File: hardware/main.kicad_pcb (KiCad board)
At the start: 4 copper layers, 57 x 93 mm, 398 parts, among them J1 DS1128-09-S8B8X, J2 DS1128-09-S8B8X, J3 DS1128-09-S8B8X, J4 98424-G52-04ALF, J5 Bus_PCI_Express_Mini, J6 IDC-08M, J7 IDC-08M, J8 USB_C_Receptacle, J9 TYPE-C-31-M-12, Q1 SSM6J501NU, Q2 SSM6J501NU, Q3 FDV301N, Q4 BC817, SW1 TS-1187A-B-A-B, SW2 TS-1187A-B-A-B, SW3 TS-1187A-B-A-B, SW4 TS-1187A-B-A-B, U1 SN74LVC1G175, U10 W25Q256FVEIG, U12 TPD2EUSB30, U13 TPD2EUSB30, U14 TPD2EUSB30, U15 IP5328P, U16 N096-2864KSWEG01-H30, U2 MT7621A, U3 TPS63020, U4 TPS63020, U5 MT3420B, U6 MT3420B, U7 MT3420B, U8 MT3420B, U9 NT5CB64M16FP-DH (!), Y1 X322540MPB4SI

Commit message: add mPCI-e and m2 conn
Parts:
- added J10: AS0BC21-S30BM-7H, MAS_Package_std:Bus_M.2_Socket_M, B.Cu at (50.2, -47.0)
- J5: footprint Connector_PCBEdge:BUS_PCI_Express_Mini_Dual -> MAS_Package_std:BUS_PCI_Express_Mini_Dual; moved to B.Cu
- moved J5 137.1 mm to (51.4, -75.6), turned to -90 degrees
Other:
- outline, holes or cut-outs redrawn

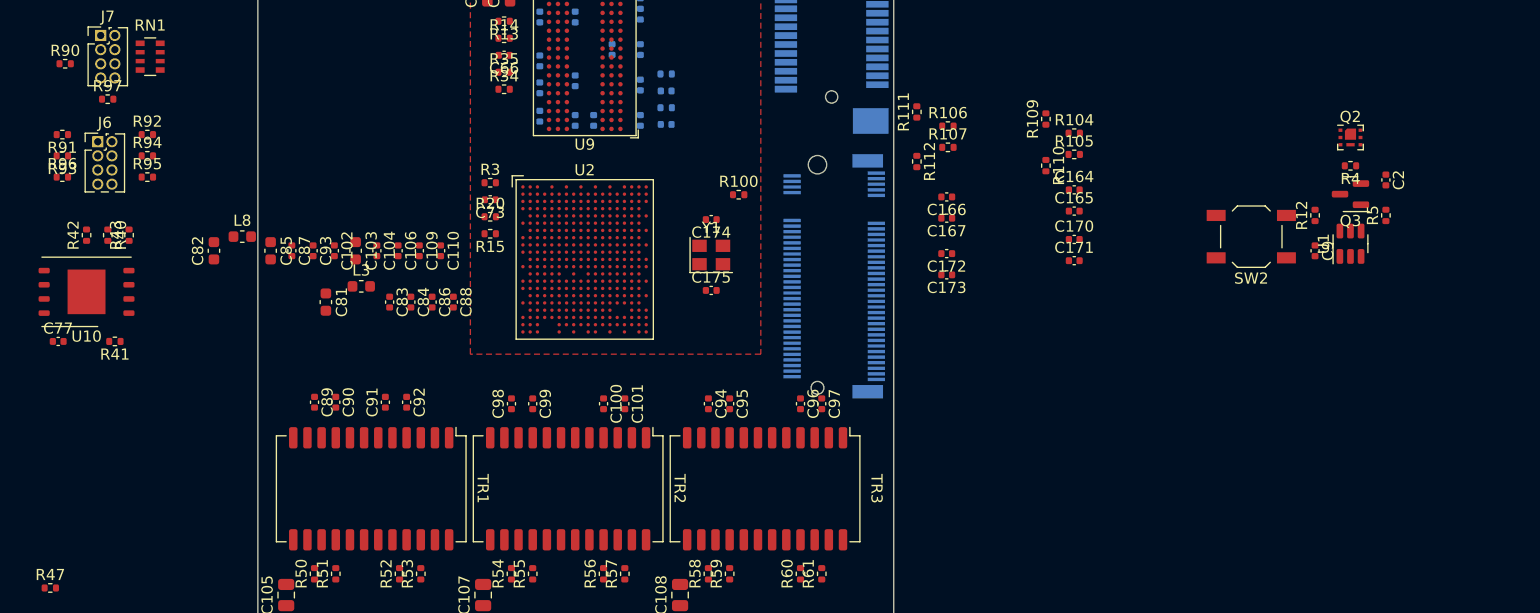
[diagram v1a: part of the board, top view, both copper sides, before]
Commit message: pinlayout for pci-e
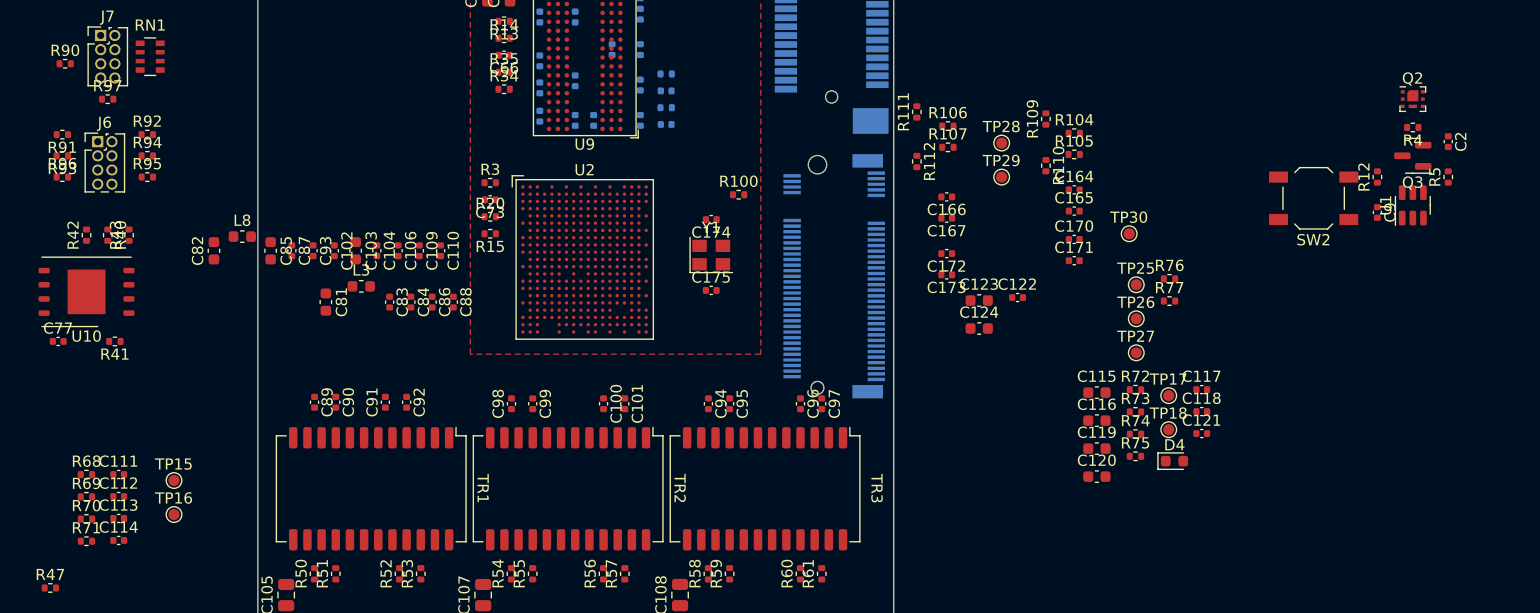
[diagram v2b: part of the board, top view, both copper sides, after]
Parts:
- added C111: 100n, Capacitor_SMD:C_0402_1005Metric, F.Cu at (-12.5, -29.2)
- added C112: 100n, Capacitor_SMD:C_0402_1005Metric, F.Cu at (-12.5, -27.2)
- added C113: 100n, Capacitor_SMD:C_0402_1005Metric, F.Cu at (-12.5, -25.3)
- added C114: 100n, Capacitor_SMD:C_0402_1005Metric, F.Cu at (-12.5, -23.3)
- added C115: 10u, Capacitor_SMD:C_0603_1608Metric, F.Cu at (75.2, -36.6)
- added C116: 10u, Capacitor_SMD:C_0603_1608Metric, F.Cu at (75.2, -34.0)
- added C117: 100n, Capacitor_SMD:C_0402_1005Metric, F.Cu at (84.6, -36.8)
- added C118: 100n, Capacitor_SMD:C_0402_1005Metric, F.Cu at (84.6, -34.9)
- added C119: 10u, Capacitor_SMD:C_0603_1608Metric, F.Cu at (75.2, -31.5)
- added C120: 10u, Capacitor_SMD:C_0603_1608Metric, F.Cu at (75.2, -29.0)
- added C121: 100n, Capacitor_SMD:C_0402_1005Metric, F.Cu at (84.6, -32.9)
- added C122: 100n, Capacitor_SMD:C_0402_1005Metric, F.Cu at (68.1, -45.1)
- added C123: 10u, Capacitor_SMD:C_0603_1608Metric, F.Cu at (64.7, -44.8)
- added C124: 10u, Capacitor_SMD:C_0603_1608Metric, F.Cu at (64.7, -42.3)
- added D4: LEDY, Diode_SMD:D_0603_1608Metric, F.Cu at (82.2, -30.4)
- added R68: 51R, Resistor_SMD:R_0402_1005Metric, F.Cu at (-15.4, -29.2)
- added R69: 0R, Resistor_SMD:R_0402_1005Metric, F.Cu at (-15.4, -27.2)
- added R70: 0R, Resistor_SMD:R_0402_1005Metric, F.Cu at (-15.4, -25.2)
- added R71: 51R, Resistor_SMD:R_0402_1005Metric, F.Cu at (-15.4, -23.2)
- added R72: 1k, Resistor_SMD:R_0402_1005Metric, F.Cu at (78.7, -36.8)
- added R73: 0R, Resistor_SMD:R_0402_1005Metric, F.Cu at (78.7, -34.8)
- added R74: 4.7k, Resistor_SMD:R_0402_1005Metric, F.Cu at (78.7, -32.8)
- added R75: 4.7k, Resistor_SMD:R_0402_1005Metric, F.Cu at (78.7, -30.9)
- added R76: 0R, Resistor_SMD:R_0402_1005Metric, F.Cu at (81.7, -46.8)
- added R77: 0R, Resistor_SMD:R_0402_1005Metric, F.Cu at (81.7, -44.8)
- added TP15: TP, TestPoint:TestPoint_Pad_D1.0mm, F.Cu at (-7.51, -28.7)
- added TP16: TP, TestPoint:TestPoint_Pad_D1.0mm, F.Cu at (-7.51, -25.6)
- added TP17: TP, TestPoint:TestPoint_Pad_D1.0mm, F.Cu at (81.7, -36.3)
- added TP18: TP, TestPoint:TestPoint_Pad_D1.0mm, F.Cu at (81.7, -33.2)
- added TP25: TP, TestPoint:TestPoint_Pad_D1.0mm, F.Cu at (78.7, -46.2)
- added TP26: TP, TestPoint:TestPoint_Pad_D1.0mm, F.Cu at (78.7, -43.2)
- added TP27: TP, TestPoint:TestPoint_Pad_D1.0mm, F.Cu at (78.7, -40.1)
- added TP28: TP, TestPoint:TestPoint_Pad_D1.0mm, F.Cu at (66.7, -58.9)
- added TP29: TP, TestPoint:TestPoint_Pad_D1.0mm, F.Cu at (66.7, -55.9)
- added TP30: TP, TestPoint:TestPoint_Pad_D1.0mm, F.Cu at (78.1, -50.8)
- J5: value Bus_PCI_Express_Mini -> miniPCI-E_52P_5.2
- moved C9 6.56 mm to (100.4, -52.7)
- moved Q2 6.56 mm to (103.5, -62.9)
- moved Q3 6.56 mm to (103.5, -57.8)
- moved R12 6.56 mm to (100.4, -55.9)
- moved R4 6.56 mm to (103.5, -60.3)
- moved U1 6.56 mm to (103.5, -53.3)
- moved C2 6.56 mm to (106.7, -59.1)
- moved R5 6.56 mm to (106.7, -55.9)
- moved SW2 6.56 mm to (94.6, -54.0)
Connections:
- C164 pad 2: /Interface/PCIE_TX1_P -> /Interface/PCIE_TX0_P
- C165 pad 2: /Interface/PCIE_TX1_N -> /Interface/PCIE_TX0_N
- C166 pad 2: /Interface/PCIE_TX0_P -> /Interface/PCIE_TX1_P
- C167 pad 2: /Interface/PCIE_TX0_N -> /Interface/PCIE_TX1_N
- C170 pad 2: /Interface/PCIE_RX1_P -> /Interface/PCIE_RX0_P
- C171 pad 2: /Interface/PCIE_RX1_N -> /Interface/PCIE_RX0_N
- C172 pad 2: /Interface/PCIE_RX0_P -> /Interface/PCIE_RX1_P
- C173 pad 2: /Interface/PCIE_RX0_N -> /Interface/PCIE_RX1_N
- J10 pad 1: Net-(J10-GND-Pad1) -> -BATT
- J10 pad 10: unconnected-(J10-DAS/~{DSS}/~{LED1}-Pad10) -> Net-(J10-DAS/~{DSS}/~{LED1})
- J10 pad 12: Net-(J10-3.3V-Pad12) -> +3V3
- J10 pad 14: Net-(J10-3.3V-Pad12) -> +3V3
- J10 pad 15: Net-(J10-GND-Pad1) -> -BATT
- J10 pad 16: Net-(J10-3.3V-Pad12) -> +3V3
- J10 pad 18: Net-(J10-3.3V-Pad12) -> +3V3
- J10 pad 2: Net-(J10-3.3V-Pad12) -> +3V3
- J10 pad 21: Net-(J10-GND-Pad1) -> -BATT
- J10 pad 27: Net-(J10-GND-Pad1) -> -BATT
- J10 pad 29: unconnected-(J10-PERn1-Pad29) -> /Interface/PCIE_RX2_N
- J10 pad 3: Net-(J10-GND-Pad1) -> -BATT
- J10 pad 31: unconnected-(J10-PERp1-Pad31) -> /Interface/PCIE_RX2_P
- J10 pad 33: Net-(J10-GND-Pad1) -> -BATT
- J10 pad 35: unconnected-(J10-PETn1-Pad35) -> /Interface/PCIE_TX2_N
- J10 pad 37: unconnected-(J10-PETp1-Pad37) -> /Interface/PCIE_TX2_P
- J10 pad 39: Net-(J10-GND-Pad1) -> -BATT
- J10 pad 4: Net-(J10-3.3V-Pad12) -> +3V3
- J10 pad 41: unconnected-(J10-PERn0/SATA-B+-Pad41) -> /Interface/PCIE_RX1_N
- J10 pad 43: unconnected-(J10-PERp0/SATA-B--Pad43) -> /Interface/PCIE_RX1_P
- J10 pad 45: Net-(J10-GND-Pad1) -> -BATT
- J10 pad 47: unconnected-(J10-PETn0/SATA-A--Pad47) -> /Interface/PCIE_TX1_N
- J10 pad 49: unconnected-(J10-PETp0/SATA-A+-Pad49) -> /Interface/PCIE_TX1_P
- J10 pad 50: unconnected-(J10-~{PERST}-Pad50) -> Net-(J10-~{PERST})
- J10 pad 51: Net-(J10-GND-Pad1) -> -BATT
- J10 pad 52: unconnected-(J10-~{CLKREQ}-Pad52) -> Net-(J10-~{CLKREQ})
- J10 pad 53: unconnected-(J10-REFCLKn-Pad53) -> /Interface/PCIE_CK1_N
- J10 pad 54: unconnected-(J10-~{PEWAKE}-Pad54) -> Net-(J10-~{PEWAKE})
- J10 pad 55: unconnected-(J10-REFCLKp-Pad55) -> /Interface/PCIE_CK1_P
- J10 pad 57: Net-(J10-GND-Pad1) -> -BATT
- J10 pad 70: Net-(J10-3.3V-Pad12) -> +3V3
- J10 pad 71: Net-(J10-GND-Pad1) -> -BATT
- J10 pad 72: Net-(J10-3.3V-Pad12) -> +3V3
- J10 pad 73: Net-(J10-GND-Pad1) -> -BATT
- J10 pad 74: Net-(J10-3.3V-Pad12) -> +3V3
- J10 pad 75: Net-(J10-GND-Pad1) -> -BATT
- J10 pad 9: Net-(J10-GND-Pad1) -> -BATT
- J5 pad 1: unconnected-(J5-~{WAKE}-Pad1) -> Net-(J5-~{WAKE})
- J5 pad 11: unconnected-(J5-REFCLK--Pad11) -> /Interface/PCIE_CK0_N
- J5 pad 13: unconnected-(J5-REFCLK+-Pad13) -> /Interface/PCIE_CK0_P
- J5 pad 15: Net-(J5-GND-Pad15) -> -BATT
- J5 pad 18: Net-(J5-GND-Pad15) -> -BATT
- J5 pad 2: unconnected-(J5-+3V3AUX-Pad2) -> +3V3
- J5 pad 20: unconnected-(J5-~{W_DISABLE}-Pad20) -> Net-(J5-~{W_DISABLE})
- J5 pad 21: Net-(J5-GND-Pad15) -> -BATT
- J5 pad 22: unconnected-(J5-~{PERST}-Pad22) -> Net-(J5-~{PERST})
- J5 pad 23: unconnected-(J5-PERn0-Pad23) -> /Interface/PCIE_RX0_N
- J5 pad 24: unconnected-(J5-+3V3AUX-Pad24) -> +3V3
- J5 pad 25: unconnected-(J5-PERp0-Pad25) -> /Interface/PCIE_RX0_P
- J5 pad 26: Net-(J5-GND-Pad15) -> -BATT
- J5 pad 27: Net-(J5-GND-Pad15) -> -BATT
- J5 pad 28: unconnected-(J5-+1V5-Pad28) -> +1V5
- J5 pad 29: Net-(J5-GND-Pad15) -> -BATT
- J5 pad 31: unconnected-(J5-PETn0-Pad31) -> /Interface/PCIE_TX0_N
- J5 pad 33: unconnected-(J5-PETp0-Pad33) -> /Interface/PCIE_TX0_P
- J5 pad 34: Net-(J5-GND-Pad15) -> -BATT
- J5 pad 35: Net-(J5-GND-Pad15) -> -BATT
- J5 pad 36: unconnected-(J5-USB_D--Pad36) -> /Interface/USB1_DP
- J5 pad 37: Net-(J5-GND-Pad15) -> -BATT
- J5 pad 38: unconnected-(J5-USB_D+-Pad38) -> /Interface/USB1_DM
- J5 pad 39: unconnected-(J5-+3V3AUX-Pad39) -> +3V3
- J5 pad 4: Net-(J5-GND-Pad15) -> -BATT
- J5 pad 40: Net-(J5-GND-Pad15) -> -BATT
- J5 pad 41: unconnected-(J5-+3V3AUX-Pad41) -> +3V3
- J5 pad 43: Net-(J5-GND-Pad15) -> -BATT
- J5 pad 44: unconnected-(J5-~{LED_WLAN}-Pad44) -> Net-(D4-A)
- J5 pad 45: unconnected-(J5-Reserved-Pad45) -> Net-(J5-Reserved-Pad45)
- J5 pad 47: unconnected-(J5-Reserved-Pad47) -> Net-(C120-Pad1)
- J5 pad 48: unconnected-(J5-+1V5-Pad48) -> +1V5
- J5 pad 49: unconnected-(J5-Reserved-Pad49) -> Net-(C120-Pad1)
- J5 pad 50: Net-(J5-GND-Pad15) -> -BATT
- J5 pad 51: unconnected-(J5-Reserved-Pad51) -> Net-(J5-Reserved-Pad51)
- J5 pad 52: unconnected-(J5-+3V3AUX-Pad52) -> +3V3
- J5 pad 6: unconnected-(J5-+1V5-Pad6) -> +1V5
- J5 pad 7: unconnected-(J5-~{CLKREQ}-Pad7) -> Net-(J5-~{CLKREQ})
- J5 pad 9: Net-(J5-GND-Pad15) -> -BATT
- J5 pad MP: unconnected-(J5-PadMP) -> -BATT
- R104 pad 1: /Interface/PCIE_CK1_P -> /Interface/PCIE_CK0_P
- R105 pad 1: /Interface/PCIE_CK1_N -> /Interface/PCIE_CK0_N
- R106 pad 1: /Interface/PCIE_CK0_P -> /Interface/PCIE_CK1_P
- R107 pad 1: /Interface/PCIE_CK0_N -> /Interface/PCIE_CK1_N
- R109 pad 1: /Interface/PCIE_CK1_P -> /Interface/PCIE_CK0_P
- R110 pad 1: /Interface/PCIE_CK1_N -> /Interface/PCIE_CK0_N
- R111 pad 1: /Interface/PCIE_CK0_P -> /Interface/PCIE_CK1_P
- R112 pad 1: /Interface/PCIE_CK0_N -> /Interface/PCIE_CK1_N
- U2 pad K1: unconnected-(U2B-USB_DM_P1-PadK1) -> /Interface/USB1_DM
- U2 pad K2: unconnected-(U2B-USB_DP_P1-PadK2) -> /Interface/USB1_DP
- U2 pad M13: unconnected-(U2B-PCIE_CKP2-PadM13) -> Net-(U2B-PCIE_CKP2)
- U2 pad M14: unconnected-(U2B-PCIE_CKN2-PadM14) -> Net-(U2B-PCIE_CKN2)
- U2 pad M17: unconnected-(U2B-PCIE_RXP2-PadM17) -> Net-(U2B-PCIE_RXP2)
- U2 pad M18: unconnected-(U2B-PCIE_RXN2-PadM18) -> Net-(U2B-PCIE_RXN2)
- U2 pad N16: unconnected-(U2B-PCIE_TXP2-PadN16) -> Net-(U2B-PCIE_TXP2)
- U2 pad N17: unconnected-(U2B-PCIE_TXN2-PadN17) -> Net-(U2B-PCIE_TXN2)

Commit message: update pcb
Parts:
- removed C193: 100n, Capacitor_SMD:C_0402_1005Metric
- removed Q4: BC817, Package_TO_SOT_SMD:SOT-23
- removed R125: 10k, Resistor_SMD:R_0402_1005Metric
- removed R126: 470R, Resistor_SMD:R_0402_1005Metric
- removed R127: 1k, Resistor_SMD:R_0402_1005Metric
- removed SW3: TS-1187A-B-A-B, Button_Switch_SMD:SW_SPST_TL3342
- C1, C10, C100, C101, C102, C103, C104, C105, C106, C107, C108, C109, C11, C110, C12, C13, C158, C159, C16, C160, C161, C162, C163, C169, C17, C177, C178, C179, C194, C2, C22, C23, C24, C26, C27, C28, C3, C32, C42, C5, C7, C78, C79, C8, C80, C81, C82, C83, C84, C85, C86, C87, C88, C89, C9, C90, C91, C92, C93, C94, C95, C96, C97, C98, C99, D3, J6, J8, J9, JP2, L3, L8, Q2, Q3, R101, R102, R113, R114, R12, R128, R129, R130, R131, R132, R133, R134, R135, R136, R137, R138, R139, R140, R141, R142, R143, R144, R145, R146, R147, R148, R149, R150, R151, R152, R153, R154, R155, R156, R157, R158, R159, R160, R18, R19, R44, R45, R46, R5, R50, R51, R52, R53, R54, R55, R56, R57, R58, R59, R60, R61, R8, R9, U1, U12, U13, U14: moved to B.Cu
- D2: value LEDG -> MBR0540; footprint Diode_SMD:D_0603_1608Metric -> Diode_SMD:D_SOD-123
- R17: value 100k -> 10k
- TP1, TP11, TP12, TP13, TP14, TP19, TP2, TP20, TP21, TP22, TP3, TP4, TP5, TP6, TP7, TP8, TP9: footprint TestPoint:TestPoint_Pad_D1.0mm -> MAS_Package_std:TestPoint_Pad_D1mm; moved to B.Cu
- TP10, TP15, TP16, TP17, TP18, TP23, TP24, TP25, TP26, TP27, TP28, TP29, TP30, TP31, TP32, TP33, TP34: footprint TestPoint:TestPoint_Pad_D1.0mm -> MAS_Package_std:TestPoint_Pad_D1mm
- moved C194 150.5 mm to (38.6, -90.3), turned to 90 degrees
- moved R128 147.2 mm to (38.6, -87.1), turned to 90 degrees
- moved D3 145.5 mm to (40.9, -87.6), turned to 90 degrees
- moved FID2 142.5 mm to (3.51, -30.9), turned to 90 degrees
- moved SW4 139.8 mm to (39.9, -88.0), turned to 90 degrees
- moved FID3 136.0 mm to (8.13, -30.6), turned to 90 degrees
- moved FID1 135.7 mm to (8.13, -35.2), turned to 90 degrees
- moved H4 121.6 mm to (10.9, -39.8)
- moved TP24 121.3 mm to (37.5, -46.7)
- moved TP23 119.4 mm to (36.6, -47.6)
- moved R98 115.5 mm to (52.7, 12.2)
- moved R99 115.5 mm to (52.7, 9.65)
- moved H1 115.2 mm to (3.17, -55.2)
- moved TP1 107.9 mm to (36.1, -58.2), turned to 0 degrees
- moved TP2 107.9 mm to (36.1, -60.1), turned to 0 degrees
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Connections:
- C34 pad 1: Net-(JP2-B) -> +5V
- C9 pad 1: Net-(U1-CLK) -> Net-(D2-K)
- D2 pad 2: Net-(D2-A) -> /Power/WPS
- H4 pad 1: GNDREF -> (no net)
- R12 pad 1: Net-(U1-CLK) -> Net-(D2-K)
- R17 pad 1: Net-(JP2-B) -> +3V3
- R17 pad 2: Net-(U3-PG) -> /Power/WPS
- SW2 pad 2: Net-(U1-CLK) -> Net-(D2-K)
- U1 pad 1: Net-(U1-CLK) -> Net-(D2-K)
- U3 pad 14: Net-(U3-PG) -> unconnected-(U3-PG-Pad14)

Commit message: circuits are combined
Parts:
- removed C158, C182, C195, C198, C199, C200, C201, C202, C203: 4.7u, Capacitor_SMD:C_0603_1608Metric
- removed C163, C176, C177, C179: 470n, Capacitor_SMD:C_0402_1005Metric
- removed C180, C181, C187, C188: 10u, Capacitor_SMD:C_0603_1608Metric
- removed R76, R77: 0R, Resistor_SMD:R_0402_1005Metric
- added C125: 10u, Capacitor_SMD:C_0603_1608Metric, F.Cu at (6.59, -63.4)
- added C126: 22p, Capacitor_SMD:C_0402_1005Metric, F.Cu at (15.9, -74.8)
- added C127: 10u, Capacitor_SMD:C_0603_1608Metric, F.Cu at (17.1, -73.5)
- added C128: 4.7u, Capacitor_SMD:C_0603_1608Metric, F.Cu at (67.5, 4.47)
- added C129: 4.7u, Capacitor_SMD:C_0603_1608Metric, F.Cu at (67.5, 6.99)
- added C130: 4.7u, Capacitor_SMD:C_0603_1608Metric, F.Cu at (67.5, 9.49)
- added C131: 4.7u, Capacitor_SMD:C_0603_1608Metric, F.Cu at (33.8, 12.8)
- added C132: 4.7u, Capacitor_SMD:C_0603_1608Metric, F.Cu at (33.8, 15.3)
- added C133: 4.7u, Capacitor_SMD:C_0603_1608Metric, F.Cu at (33.8, 17.8)
- added C134: 4.7u, Capacitor_SMD:C_0603_1608Metric, B.Cu at (43.5, -56.4)
- added C135: 4.7u, Capacitor_SMD:C_0603_1608Metric, B.Cu at (43.5, -53.9)
- added C136: 4.7u, Capacitor_SMD:C_0603_1608Metric, B.Cu at (42.9, -47.6)
- added C137: 4.7u, Capacitor_SMD:C_0603_1608Metric, F.Cu at (88.4, 2.29)
- added C138: 4.7u, Capacitor_SMD:C_0603_1608Metric, F.Cu at (86.2, 9.14)
- added C139: 4.7u, Capacitor_SMD:C_0603_1608Metric, B.Cu at (16.1, -42.8)
- added C140: 470n, Capacitor_SMD:C_0402_1005Metric, B.Cu at (31.4, -45.7)
- added C141: 470n, Capacitor_SMD:C_0402_1005Metric, B.Cu at (36.9, -50.7)
- added R125: 10k, Resistor_SMD:R_0402_1005Metric, B.Cu at (34.8, -83.1)
- added R87: 4.7k, Resistor_SMD:R_0402_1005Metric, F.Cu at (51.1, -60.2)
- C103, C14, C15, C30, C31, C75, C76, C81, C82, C85: value 4.7u -> 10u
- C116, C23, C45, C46, C5, C6: value 10u -> 4.7u
- C168, C47: moved to B.Cu
- C52: value 22p -> 4.7u; footprint Capacitor_SMD:C_0402_1005Metric -> Capacitor_SMD:C_0603_1608Metric
- C55, C56: value 10u -> 470n; footprint Capacitor_SMD:C_0603_1608Metric -> Capacitor_SMD:C_0402_1005Metric; moved to B.Cu
- D2: value MBR0540 -> LEDY; footprint Diode_SMD:D_SOD-123 -> Diode_SMD:D_0603_1608Metric
- D4: value LEDY -> MBR0540; footprint Diode_SMD:D_0603_1608Metric -> Diode_SMD:D_SOD-123; moved to B.Cu
- R17: value 10k -> 0R
- R72: value 1k -> 0R
- R75: value 4.7k -> 1k
- moved C5 55.9 mm to (2.67, -72.5)
- moved C32 54.1 mm to (55.1, -90.2)
- moved C33 41.8 mm to (5.97, -70.5)
- moved C55 36.0 mm to (37.0, -53.0), turned to 180 degrees
- moved C47 33.5 mm to (39.6, -58.3), turned to 180 degrees
- moved C56 31.8 mm to (42.2, -50.5)
- moved D4 31.4 mm to (34.4, -79.3), turned to 0 degrees
- moved C168 15.0 mm to (30.9, -44.3), turned to 180 degrees
- moved C52 13.0 mm to (23.6, -84.1)
- moved C30 11.4 mm to (11.8, -58.9)
- moved C50 0.32 mm to (16.4, -70.4)
- moved C48 0.32 mm to (18.2, -67.9)
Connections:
- net /Charger/CC1 renamed /CC1
- net /Charger/CC2 renamed /CC2
- net /Charger/DMC renamed /DMC
- net /Charger/DPC renamed /DPC
- net /Charger/KEY renamed /KEY
- net /Charger/VBUSG renamed /VBUSG
- net /Charger/VMID renamed /VMID
- net /Charger/VSYS renamed /VSYS
- net /Ethernet/EN_DC renamed /EN_DC
- net /Ethernet/ESW_TXVN_A_P2 renamed /ESW_TXVN_A_P2
- net /Ethernet/ESW_TXVN_A_P3 renamed /ESW_TXVN_A_P3
- net /Ethernet/ESW_TXVN_A_P4 renamed /ESW_TXVN_A_P4
- net /Ethernet/ESW_TXVN_B_P2 renamed /ESW_TXVN_B_P2
- net /Ethernet/ESW_TXVN_B_P3 renamed /ESW_TXVN_B_P3
- net /Ethernet/ESW_TXVN_B_P4 renamed /ESW_TXVN_B_P4
- net /Ethernet/ESW_TXVN_C_P2 renamed /ESW_TXVN_C_P2
- net /Ethernet/ESW_TXVN_C_P3 renamed /ESW_TXVN_C_P3
- net /Ethernet/ESW_TXVN_C_P4 renamed /ESW_TXVN_C_P4
- net /Ethernet/ESW_TXVN_D_P2 renamed /ESW_TXVN_D_P2
- net /Ethernet/ESW_TXVN_D_P3 renamed /ESW_TXVN_D_P3
- net /Ethernet/ESW_TXVN_D_P4 renamed /ESW_TXVN_D_P4
- net /Ethernet/ESW_TXVP_A_P2 renamed /ESW_TXVP_A_P2
- net /Ethernet/ESW_TXVP_A_P3 renamed /ESW_TXVP_A_P3
- net /Ethernet/ESW_TXVP_A_P4 renamed /ESW_TXVP_A_P4
- net /Ethernet/ESW_TXVP_B_P2 renamed /ESW_TXVP_B_P2
- net /Ethernet/ESW_TXVP_B_P3 renamed /ESW_TXVP_B_P3
- net /Ethernet/ESW_TXVP_B_P4 renamed /ESW_TXVP_B_P4
- net /Ethernet/ESW_TXVP_C_P2 renamed /ESW_TXVP_C_P2
- net /Ethernet/ESW_TXVP_C_P3 renamed /ESW_TXVP_C_P3
- net /Ethernet/ESW_TXVP_C_P4 renamed /ESW_TXVP_C_P4
- net /Ethernet/ESW_TXVP_D_P2 renamed /ESW_TXVP_D_P2
- net /Ethernet/ESW_TXVP_D_P3 renamed /ESW_TXVP_D_P3
- net /Ethernet/ESW_TXVP_D_P4 renamed /ESW_TXVP_D_P4
- net /Ethernet/P2A_N renamed /P2A_N
- net /Ethernet/P2A_P renamed /P2A_P
- net /Ethernet/P2B_N renamed /P2B_N
- net /Ethernet/P2B_P renamed /P2B_P
- net /Ethernet/P2C_N renamed /P2C_N
- net /Ethernet/P2C_P renamed /P2C_P
- net /Ethernet/P2D_N renamed /P2D_N
- net /Ethernet/P2D_P renamed /P2D_P
- net /Ethernet/P3A_N renamed /P3A_N
- net /Ethernet/P3A_P renamed /P3A_P
- net /Ethernet/P3B_N renamed /P3B_N
- net /Ethernet/P3B_P renamed /P3B_P
- net /Ethernet/P3C_N renamed /P3C_N
- net /Ethernet/P3C_P renamed /P3C_P
- net /Ethernet/P3D_N renamed /P3D_N
- net /Ethernet/P3D_P renamed /P3D_P
- net /Ethernet/P4A_N renamed /P4A_N
- net /Ethernet/P4A_P renamed /P4A_P
- net /Ethernet/P4B_N renamed /P4B_N
- net /Ethernet/P4B_P renamed /P4B_P
- net /Ethernet/P4C_N renamed /P4C_N
- net /Ethernet/P4C_P renamed /P4C_P
- net /Ethernet/P4D_N renamed /P4D_N
- net /Ethernet/P4D_P renamed /P4D_P
- net /Ethernet/POWER_LED renamed /POWER_LED
- net /Ethernet/Y0- renamed /Y0-
- net /Ethernet/Y1- renamed /Y1-
- net /Ethernet/Y2- renamed /Y2-
- net /Ethernet/Y3- renamed /Y3-
- net /Ethernet/Y4- renamed /Y4-
- net /Interface/CTS2 renamed /CTS2
- net /Interface/PCIE_CK0_N renamed /PCIE_CK0_N
- net /Interface/PCIE_CK0_P renamed /PCIE_CK0_P
- net /Interface/PCIE_CK1_N renamed /PCIE_CK1_N
- net /Interface/PCIE_CK1_P renamed /PCIE_CK1_P
- net /Interface/PCIE_CK2_N renamed /PCIE_CK2_N
- net /Interface/PCIE_CK2_P renamed /PCIE_CK2_P
- net /Interface/PCIE_RX0_N renamed /PCIE_RX0_N
- net /Interface/PCIE_RX0_P renamed /PCIE_RX0_P
- net /Interface/PCIE_RX1_N renamed /PCIE_RX1_N
- net /Interface/PCIE_RX1_P renamed /PCIE_RX1_P
- net /Interface/PCIE_RX2_N renamed /PCIE_RX2_N
- net /Interface/PCIE_RX2_P renamed /PCIE_RX2_P
- net /Interface/PCIE_TX0_N renamed /PCIE_TX0_N
- net /Interface/PCIE_TX0_P renamed /PCIE_TX0_P
- net /Interface/PCIE_TX1_N renamed /PCIE_TX1_N
- net /Interface/PCIE_TX1_P renamed /PCIE_TX1_P
- net /Interface/PCIE_TX2_N renamed /PCIE_TX2_N
- net /Interface/PCIE_TX2_P renamed /PCIE_TX2_P
- net /Interface/RTS2 renamed /RTS2
- net /Interface/SSUSB_RXN renamed /SSUSB_RXN
- net /Interface/SSUSB_RXP renamed /SSUSB_RXP
- net /Interface/SSUSB_TXN renamed /SSUSB_TXN
- net /Interface/SSUSB_TXP renamed /SSUSB_TXP
- net /Interface/UART0_RXD renamed /UART0_RXD
- net /Interface/UART0_TXD renamed /UART0_TXD
- net /Interface/UART1_RXD renamed /UART1_RXD
- net /Interface/UART1_TXD renamed /UART1_TXD
- net /Interface/USB1_DM renamed /USB1_DM
- net /Interface/USB1_DP renamed /USB1_DP
- net /Interface/USB_DM renamed /USB_DM
- net /Interface/USB_DP renamed /USB_DP
- net /Memory/DDR3RSTB renamed /DDR3RSTB
- net /Memory/DDR_VREF1 renamed /DDR_VREF1
- net /Memory/DDR_VREF2 renamed /DDR_VREF2
- net /Memory/ND_D4 renamed /ND_D4
- net /Memory/ND_D5 renamed /ND_D5
- net /Memory/ND_D6 renamed /ND_D6
- net /Memory/ND_D7 renamed /ND_D7
- net /Memory/RA0 renamed /RA0
- net /Memory/RA1 renamed /RA1
- net /Memory/RA10 renamed /RA10
- net /Memory/RA11 renamed /RA11
- net /Memory/RA12 renamed /RA12
- net /Memory/RA13 renamed /RA13
- net /Memory/RA14 renamed /RA14
- net /Memory/RA2 renamed /RA2
- net /Memory/RA3 renamed /RA3
- net /Memory/RA4 renamed /RA4
- net /Memory/RA5 renamed /RA5
- net /Memory/RA6 renamed /RA6
- net /Memory/RA7 renamed /RA7
- net /Memory/RA8 renamed /RA8
- net /Memory/RA9 renamed /RA9
- net /Memory/RBA0 renamed /RBA0
- net /Memory/RBA1 renamed /RBA1
- net /Memory/RBA2 renamed /RBA2
- net /Memory/RCKE renamed /RCKE
- net /Memory/RCLK renamed /RCLK
- net /Memory/RDQ0 renamed /RDQ0
- net /Memory/RDQ1 renamed /RDQ1
- net /Memory/RDQ10 renamed /RDQ10
- net /Memory/RDQ11 renamed /RDQ11
- net /Memory/RDQ12 renamed /RDQ12
- net /Memory/RDQ13 renamed /RDQ13
- net /Memory/RDQ14 renamed /RDQ14
- net /Memory/RDQ15 renamed /RDQ15
- net /Memory/RDQ2 renamed /RDQ2
- net /Memory/RDQ3 renamed /RDQ3
- net /Memory/RDQ4 renamed /RDQ4
- net /Memory/RDQ5 renamed /RDQ5
- net /Memory/RDQ6 renamed /RDQ6
- net /Memory/RDQ7 renamed /RDQ7
- net /Memory/RDQ8 renamed /RDQ8
- net /Memory/RDQ9 renamed /RDQ9
- net /Memory/RDQM0 renamed /RDQM0
- net /Memory/RDQM1 renamed /RDQM1
- net /Memory/RDQS0 renamed /RDQS0
- net /Memory/RDQS1 renamed /RDQS1
- net /Memory/RODT renamed /RODT
- net /Memory/~{RCAS} renamed /~{RCAS}
- net /Memory/~{RCLK} renamed /~{RCLK}
- net /Memory/~{RCS} renamed /~{RCS}
- net /Memory/~{RDQS0} renamed /~{RDQS0}
- net /Memory/~{RDQS1} renamed /~{RDQS1}
- net /Memory/~{RRAS} renamed /~{RRAS}
- net /Memory/~{RWE} renamed /~{RWE}
- net /Other/3V3O renamed /3V3O
- C1 pad 1: +1V1 -> VD
- C103 pad 1: +1V0 -> +1V5
- C103 pad 2: Net-(C102-Pad2) -> -BATT
- C115 pad 1: +3V3 -> +1V0
- C116 pad 1: +3V3 -> +1V5
- C119 pad 1: +1V5 -> +BATT
- C120 pad 1: Net-(C120-Pad1) -> /VBUS
- C121 pad 1: Net-(C120-Pad1) -> Net-(C121-Pad1)
- C123 pad 1: +3V3 -> -BATT
- C123 pad 2: -BATT -> +BATT
- C124 pad 1: +3V3 -> +BATT
- C14 pad 1: VD -> +3V3
- C17 pad 1: +1V0 -> VD
- C194 pad 1: /Other/D2DB_PORST_N -> /D2DB_PORST_N
- C23 pad 1: +1V5 -> VD
- C30 pad 1: Net-(JP2-B) -> Net-(JP5-B)
- C31 pad 1: Net-(JP3-B) -> +3V3
- C32 pad 1: Net-(JP2-B) -> Net-(JP3-B)
- C33 pad 1: Net-(JP3-B) -> Net-(JP2-B)
- C45 pad 1: Net-(JP4-B) -> Net-(JP3-B)
- C46 pad 1: Net-(JP5-B) -> +1V5
- C52 pad 1: Net-(JP7-B) -> -BATT
- C52 pad 2: Net-(U8-FB) -> /VREG
- C55 pad 1: Net-(JP6-B) -> -BATT
- C55 pad 2: -BATT -> +3V3
- C56 pad 1: Net-(JP7-B) -> -BATT
- C56 pad 2: -BATT -> Net-(U2B-AVDD12_PE)
- C6 pad 1: VD -> Net-(JP2-B)
- C7 pad 1: VD -> Net-(JP4-B)
- C73 pad 1: /Memory/DDRVREF -> /DDRVREF
- C76 pad 1: +1V5 -> Net-(C121-Pad1)
- C82 pad 1: +1V0 -> +3V3
- C82 pad 2: Net-(C102-Pad2) -> -BATT
- C85 pad 1: +1V0 -> +1V1
- C85 pad 2: Net-(C102-Pad2) -> -BATT
- C9 pad 1: Net-(D2-K) -> Net-(D4-K)
- D2 pad 2: /Power/WPS -> Net-(D2-A)
- D3 pad 2: /Other/D2DB_PORST_N -> /D2DB_PORST_N
- D4 pad 2: Net-(D4-A) -> /WPS
- J1 pad 9: /Ethernet/G2- -> /G2-
- J2 pad 9: /Ethernet/G3- -> /G3-
- J3 pad 9: /Ethernet/G4- -> /G4-
- J5 pad 44: Net-(D4-A) -> Net-(D2-A)
- J5 pad 47: Net-(C120-Pad1) -> Net-(C121-Pad1)
- J5 pad 49: Net-(C120-Pad1) -> Net-(C121-Pad1)
- J7 pad 2: /Interface/D2DB_PORST_N -> /D2DB_PORST_N
- J9 pad A4: /Charger/VBUS -> /VBUS
- J9 pad A9: /Charger/VBUS -> /VBUS
- J9 pad B4: /Charger/VBUS -> /VBUS
- J9 pad B9: /Charger/VBUS -> /VBUS
- JP1 pad 2: /Charger/VBUS -> /VBUS
- Q1 pad 1: /Charger/VBUS -> /VBUS
- Q1 pad 2: /Charger/VBUS -> /VBUS
- Q1 pad 5: /Charger/VBUS -> /VBUS
- Q1 pad 6: /Charger/VBUS -> /VBUS
- Q1 pad 8: /Charger/VBUS -> /VBUS
- R12 pad 1: Net-(D2-K) -> Net-(D4-K)
- R121 pad 1: /Charger/INT -> /INT
- R121 pad 2: /Charger/VREG -> /VREG
- R122 pad 1: /Charger/SDA -> /SDA
- R122 pad 2: /Charger/VREG -> /VREG
- R123 pad 1: /Charger/SCL -> /SCL
- R123 pad 2: /Charger/VREG -> /VREG
- R128 pad 2: /Other/D2DB_PORST_N -> /D2DB_PORST_N
- R129 pad 2: /Other/ND_RE_N -> /ND_RE_N
- R130 pad 2: /Other/ND_RE_N -> /ND_RE_N
- R131 pad 2: /Other/ND_WE_N -> /ND_WE_N
- R132 pad 2: /Other/ND_WE_N -> /ND_WE_N
- R133 pad 2: /Other/ND_CS_N -> /ND_CS_N
- R134 pad 2: /Other/ND_CS_N -> /ND_CS_N
- R135 pad 2: /Other/MDC -> /MDC
- R136 pad 2: /Other/MDC -> /MDC
- R137 pad 2: /Other/PERST_N -> /PERST_N
- R138 pad 2: /Other/PERST_N -> /PERST_N
- R139 pad 2: /Other/TXD2 -> /TXD2
- R140 pad 2: /Other/TXD2 -> /TXD2
- R141 pad 2: /Other/RTS2_N -> /RTS2_N
- R142 pad 2: /Other/RTS2_N -> /RTS2_N
- R143 pad 2: /Other/RTS3_N -> /RTS3_N
- R144 pad 2: /Other/RTS3_N -> /RTS3_N
- R145 pad 2: /Other/TXD1 -> /TXD1
- R146 pad 2: /Other/TXD1 -> /TXD1
- R147 pad 2: /Other/GPIO0 -> /GPIO0
- R148 pad 2: /Other/GPIO0 -> /GPIO0
- R149 pad 2: /Other/P0_LED_0 -> /P0_LED_0
- R15 pad 1: /Memory/DDRVREF -> /DDRVREF
- R150 pad 2: /Other/P0_LED_0 -> /P0_LED_0
- R151 pad 2: /Other/P1_LED_0 -> /P1_LED_0
- R152 pad 2: /Other/P1_LED_0 -> /P1_LED_0
- R153 pad 2: /Other/P2_LED_0 -> /G2-
- R154 pad 2: /Other/P2_LED_0 -> /G2-
- R155 pad 2: /Other/P0_LED_1 -> /P0_LED_1
- R156 pad 2: /Other/P0_LED_1 -> /P0_LED_1
- R157 pad 2: /Other/P3_LED_0 -> /G3-
- R158 pad 2: /Other/P3_LED_0 -> /G3-
- R159 pad 2: /Other/P4_LED_0 -> /G4-
- R160 pad 2: /Other/P4_LED_0 -> /G4-
- R162 pad 2: /Other/PERST_N -> /PERST_N
- R166 pad 1: /Other/SDA -> /SDA
- R167 pad 1: /Other/SCL -> /SCL
- R17 pad 1: +3V3 -> Net-(U2A-DVDD_VREF)
- R17 pad 2: /Power/WPS -> /DDRVREF
- R20 pad 2: /Memory/DDRVREF -> /DDRVREF
- R3 pad 1: Net-(U2A-DVDD_VREF) -> Net-(C121-Pad1)
- R3 pad 2: /Memory/DDRVREF -> +5V
- R41 pad 1: /Memory/ND_CS_N -> /ND_CS_N
- R72 pad 1: -BATT -> /PERST_N
- R72 pad 2: Net-(D4-K) -> Net-(J5-~{PERST})
- R73 pad 1: Net-(C120-Pad1) -> /PERST_N
- R73 pad 2: +5V -> Net-(J10-~{PERST})
- R75 pad 1: Net-(J10-~{PERST}) -> -BATT
- R75 pad 2: +3V3 -> Net-(D2-K)
- R91 pad 2: /Interface/TXD1 -> /TXD1
- R93 pad 2: /Interface/TXD2 -> /TXD2
- R96 pad 2: /Interface/RTS2_N -> /RTS2_N
- R98 pad 2: /Interface/SCL -> /SCL
- R99 pad 1: /Interface/SDA -> /SDA
- SW2 pad 2: Net-(D2-K) -> Net-(D4-K)
- SW4 pad 1: /Other/D2DB_PORST_N -> /D2DB_PORST_N
- TP22 pad 1: /Interface/RTS3_N -> /RTS3_N
- TP32 pad 1: /Other/SDA -> /SDA
- TP33 pad 1: /Other/SCL -> /SCL
- TP34 pad 1: /Other/INT -> /INT
- U1 pad 1: Net-(D2-K) -> Net-(D4-K)
- U10 pad 1: /Memory/ND_CS_N -> /ND_CS_N
- U10 pad 6: /Memory/ND_RE_N -> /ND_RE_N
- U15 pad 11: /Charger/SCL -> /SCL
- U15 pad 12: /Charger/SDA -> /SDA
- U15 pad 13: /Charger/INT -> /INT
- U15 pad 27: /Charger/VREG -> /VREG
- U15 pad 32: /Charger/VBUS -> /VBUS
- U16 pad 18: /Other/SCL -> /SCL
- U16 pad 19: /Other/SDA -> /SDA
- U16 pad 20: /Other/SDA -> /SDA
- U2 pad AA15: /Ethernet/G3- -> /G3-
- U2 pad AA17: /Ethernet/P0_LED_0 -> /P0_LED_0
- U2 pad F3: /Memory/ND_RE_N -> /ND_RE_N
- U2 pad G14: /Interface/PERST_N -> /PERST_N
- U2 pad G15: /Interface/WPS -> /WPS
- U2 pad G2: /Memory/ND_CS_N -> /ND_CS_N
- U2 pad G4: /Memory/ND_WE_N -> /ND_WE_N
- U2 pad H2: /Interface/TXD2 -> /TXD2
- U2 pad J3: /Interface/RTS2_N -> /RTS2_N
- U2 pad J4: /Interface/RTS3_N -> /RTS3_N
- U2 pad P12: /Interface/GPIO0 -> /GPIO0
- U2 pad R12: /Interface/D2DB_PORST_N -> /D2DB_PORST_N
- U2 pad R14: /Interface/TXD1 -> /TXD1
- U2 pad T15: /Ethernet/MDC -> /MDC
- U2 pad V18: /Ethernet/INT -> /INT
- U2 pad W15: /Ethernet/G2- -> /G2-
- U2 pad W16: /Ethernet/P0_LED_1 -> /P0_LED_1
- U2 pad Y15: /Ethernet/G4- -> /G4-
- U2 pad Y16: /Ethernet/P1_LED_0 -> /P1_LED_0
- U4 pad 14: /Power/PG -> /D2DB_PORST_N

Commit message: update 100923
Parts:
- removed C133, C137, C138: 4.7u, Capacitor_SMD:C_0603_1608Metric
- removed C197: 100n, Capacitor_SMD:C_0402_1005Metric
- removed R162, R172: ~, Resistor_SMD:R_0402_1005Metric
- removed R163, R166, R167: 4.7k, Resistor_SMD:R_0402_1005Metric
- removed R164: 910k, Resistor_SMD:R_0402_1005Metric
- removed R165, R168, R169, R170, R171, R98, R99: 0R, Resistor_SMD:R_0402_1005Metric
- removed SW4: TS-1187A-B-A-B, Button_Switch_SMD:SW_SPST_TL3342
- removed TP20, TP21, TP22, TP32, TP33, TP34: TP, MAS_Package_std:TestPoint_Pad_D1mm
- removed U16: N096-2864KSWEG01-H30, MAS_Package_nostd:SSD1306-oled-0.96
- added R76: 22R, Resistor_SMD:R_0402_1005Metric, B.Cu at (45.0, -44.3)
- added R77: 22R, Resistor_SMD:R_0402_1005Metric, B.Cu at (45.0, -42.3)
- added R78: 22R, Resistor_SMD:R_0402_1005Metric, B.Cu at (45.0, -40.3)
- added R79: 22R, Resistor_SMD:R_0402_1005Metric, B.Cu at (45.0, -38.4)
- added R80: 0R, Resistor_SMD:R_0402_1005Metric, F.Cu at (33.1, -31.6)
- added R81: 0R, Resistor_SMD:R_0402_1005Metric, F.Cu at (35.1, -31.6)
- added R82: 0R, Resistor_SMD:R_0402_1005Metric, F.Cu at (37.1, -31.6)
- added R83: 0R, Resistor_SMD:R_0402_1005Metric, F.Cu at (39.1, -31.6)
- added R84: 4.7k, Resistor_SMD:R_0402_1005Metric, F.Cu at (41.1, -31.6)
- added R85: 4.7k, Resistor_SMD:R_0402_1005Metric, F.Cu at (43.1, -31.6)
- added R86: 4.7k, Resistor_SMD:R_0402_1005Metric, F.Cu at (12.7, -32.2)
- C128: moved to B.Cu
- C129: value 4.7u -> 1u
- C130: value 4.7u -> 100n; footprint Capacitor_SMD:C_0603_1608Metric -> Capacitor_SMD:C_0402_1005Metric
- C9: value 100n -> 1u; footprint Capacitor_SMD:C_0402_1005Metric -> Capacitor_SMD:C_0603_1608Metric; moved to F.Cu
- R12: value 1k -> ~; moved to F.Cu
- TP19: moved to F.Cu
- U1: value SN74LVC1G175 -> SSD1306-OLED-0.91; footprint Package_TO_SOT_SMD:SOT-23-6 -> MAS_Package_nostd:SSD1306-oled-0.91; moved to F.Cu
- moved C196 91.3 mm to (1.52, -40.5), turned to 90 degrees
- moved R161 87.0 mm to (1.52, -37.3), turned to 90 degrees
- moved C129 79.1 mm to (3.27, -39.3)
- moved C130 79.1 mm to (3.27, -36.8)
- moved R95 62.7 mm to (37.8, -89.1)
- moved R96 62.7 mm to (42.4, -89.1)
- moved J6 62.7 mm to (40.8, -91.7)
- moved R91 62.7 mm to (42.4, -91.7)
- moved R92 62.7 mm to (37.8, -91.7)
- moved R93 62.7 mm to (42.4, -90.4)
- moved R94 62.7 mm to (37.8, -90.4)
- moved C128 57.3 mm to (40.0, -45.8), turned to 180 degrees
- moved C131 56.1 mm to (2.91, -34.0)
- moved C132 56.1 mm to (2.91, -31.5)
- moved C9 54.8 mm to (9.27, -33.9), turned to 0 degrees
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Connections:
- net /CTS2 renamed /UART1_CTS
- net /INT renamed /PB_INT
- net /RTS2 renamed /UART1_RTS
- net /SCL renamed Net-(U15-L1)
- net /SDA renamed Net-(U15-L2)
- C129 pad 1: Net-(U16-C2N) -> Net-(U1-C1N)
- C129 pad 2: Net-(U16-C2P) -> Net-(U1-C1P)
- C130 pad 1: Net-(U16-C1N) -> Net-(U1-RES#)
- C130 pad 2: Net-(U16-C1P) -> -BATT
- C131 pad 1: /3V3O -> Net-(U1-VBAT)
- C132 pad 1: -BATT -> Net-(U1-VCOMH)
- C132 pad 2: /3V3O -> -BATT
- C196 pad 1: /3V3O -> Net-(U1-VBAT)
- C9 pad 1: Net-(D4-K) -> Net-(U1-C2P)
- C9 pad 2: -BATT -> Net-(U1-C2N)
- J10 pad 30: unconnected-(J10-NC-Pad30) -> /UART3_RTS
- J10 pad 32: unconnected-(J10-NC-Pad32) -> /UART3_CTS
- J10 pad 34: unconnected-(J10-NC-Pad34) -> /UART3_RXD
- J10 pad 36: unconnected-(J10-NC-Pad36) -> /UART3_TXD
- J10 pad 56: unconnected-(J10-NC-Pad56) -> Net-(J10-NC-Pad56)
- J10 pad 58: unconnected-(J10-NC-Pad58) -> Net-(J10-NC-Pad58)
- Q2 pad 3: Net-(Q2-G1) -> Net-(D4-K)
- Q3 pad 3: Net-(Q2-G1) -> Net-(D4-K)
- R12 pad 1: Net-(D4-K) -> Net-(U1-RES#)
- R12 pad 2: +BATT -> /PERST_N
- R161 pad 1: /3V3O -> Net-(U1-VBAT)
- R4 pad 2: Net-(Q2-G1) -> Net-(D4-K)
- R5 pad 1: Net-(U1-Q) -> /POWER_LED
- TP19 pad 1: Net-(U2B-TXD3) -> Net-(D4-K)
- U1 pad 1: Net-(D4-K) -> Net-(U1-C2P)
- U1 pad 2: -BATT -> Net-(U1-C2N)
- U1 pad 3: Net-(Q2-G1) -> Net-(U1-C1P)
- U1 pad 4: Net-(U1-Q) -> Net-(U1-C1N)
- U1 pad 5: +BATT -> Net-(U1-VBAT)
- U1 pad 6: -BATT -> unconnected-(U1-N.C.-Pad6)
- U2 pad P13: Net-(U2B-I2C_SCLK) -> /I2C_SCL
- U2 pad P14: Net-(U2B-I2C_SD) -> /I2C_SDA
